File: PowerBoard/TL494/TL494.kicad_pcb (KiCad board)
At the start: 2 copper layers, 50 x 75 mm, 41 parts, among them J1 AuxConn, J2 POWER_SW, Q1 STD11N65M2, U2 LT8316EFE#PBF

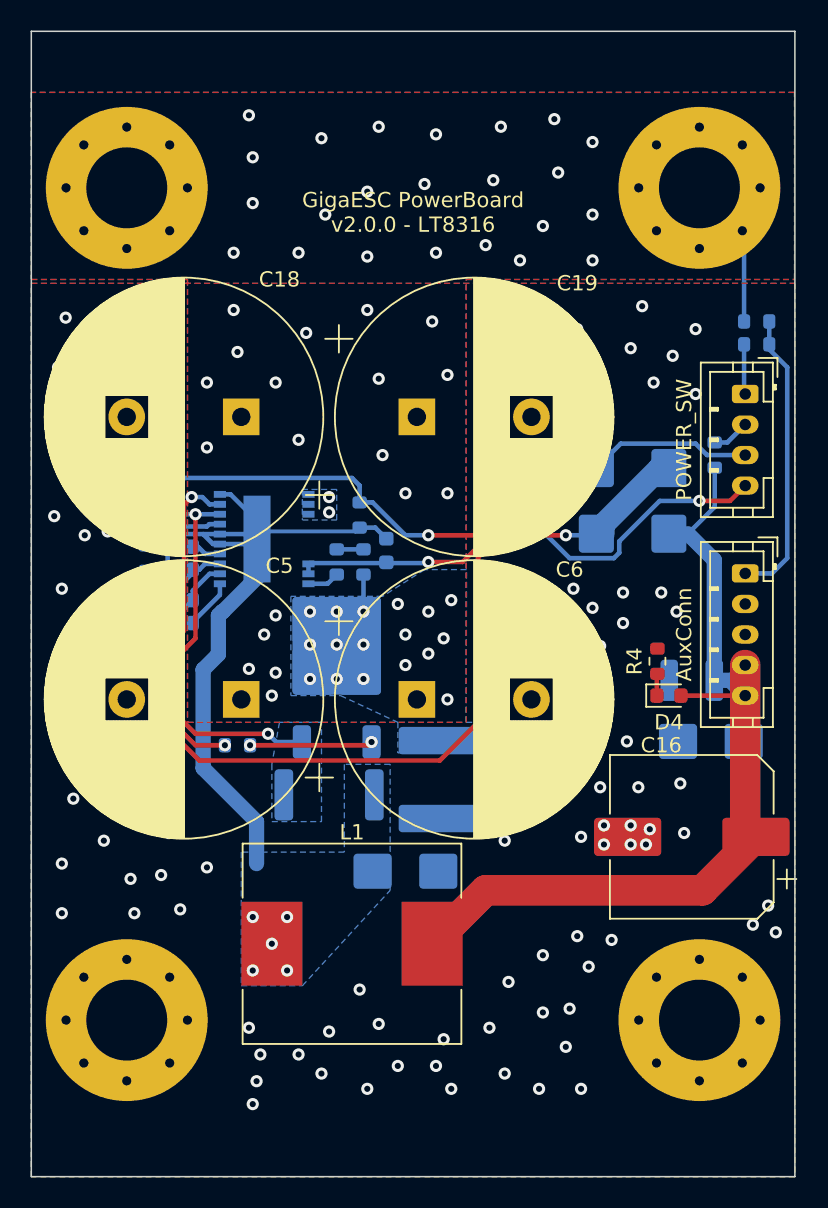
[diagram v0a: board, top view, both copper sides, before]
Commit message: v3.0.1 - GaN redesign
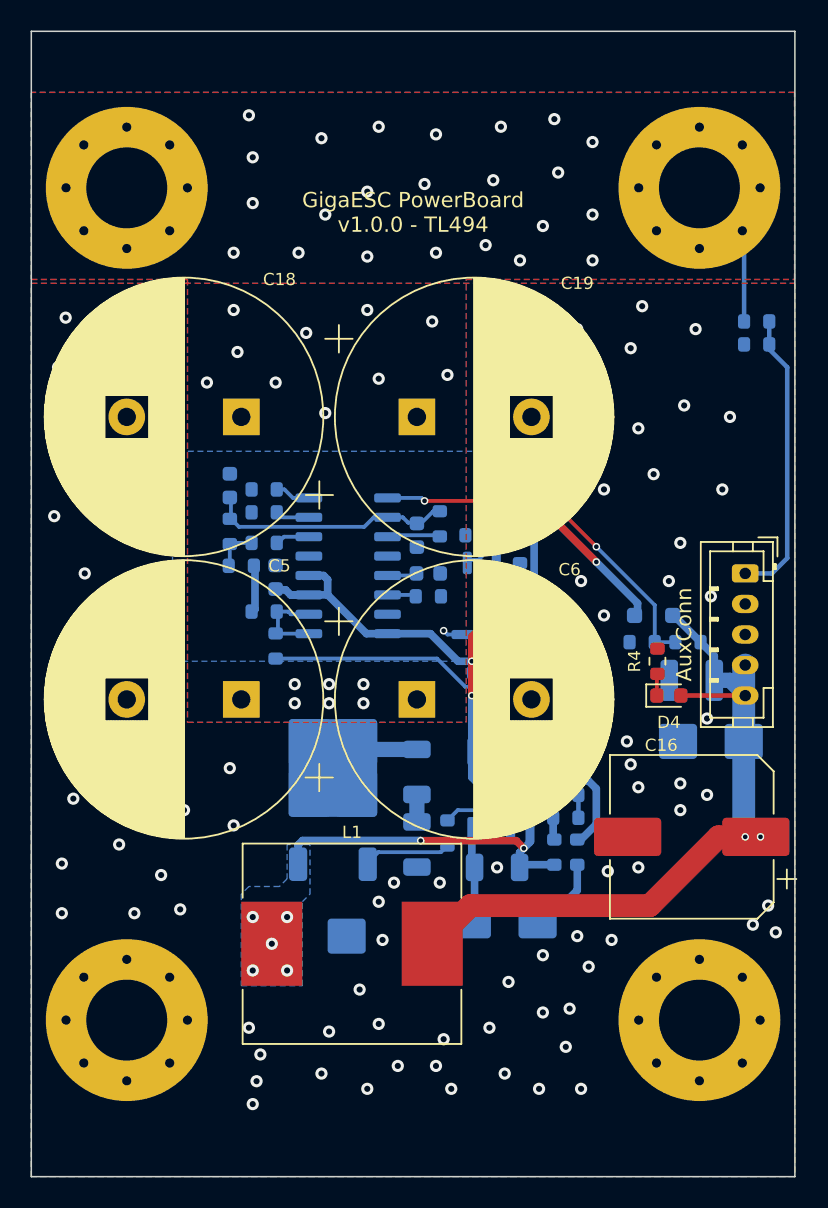
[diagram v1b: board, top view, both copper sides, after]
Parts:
- removed C10: 47p, GigaVescLibs:C_0603_1608Metric_L
- removed C13: 1n, Capacitor_SMD:C_0603_1608Metric
- removed J2: POWER_SW, Connector_JST:JST_PH_B4B-PH-K_1x04_P2.00mm_Vertical
- removed Q1: STD11N65M2, Package_TO_SOT_SMD:TO-252-2
- removed U2: LT8316EFE#PBF, GigaVescLibs:IC_LT8316EFE#PBF
- added C11: 1u, Capacitor_SMD:C_0603_1608Metric, B.Cu at (79.8, 117.0)
- added C3: 1n, Capacitor_SMD:C_0603_1608Metric, B.Cu at (76.0, 110.5)
- added C4: 100n, Capacitor_SMD:C_0603_1608Metric, B.Cu at (66.0, 110.8)
- added D3: BZT52C5V1S, Diode_SMD:D_SOD-323_HandSoldering, B.Cu at (82.5, 112.5)
- added Q2: BSS126, Package_TO_SOT_SMD:SOT-23, B.Cu at (79.2, 114.5)
- added Q5: IRFR13N20DTRPBF, Package_TO_SOT_SMD:TO-252-2, B.Cu at (69.8, 124.5)
- added R16: 10k, Resistor_SMD:R_0603_1608Metric, B.Cu at (82.0, 109.0)
- added R17: 100, Resistor_SMD:R_0603_1608Metric, B.Cu at (82.8, 115.5)
- added R18: 10k, Resistor_SMD:R_0603_1608Metric, B.Cu at (79.2, 108.0)
- added R19: 30k, Resistor_SMD:R_0603_1608Metric, B.Cu at (80.8, 105.0)
- added R20: 10k, Resistor_SMD:R_0603_1608Metric, B.Cu at (93.0, 115.0)
- added R21: 2.7k, Resistor_SMD:R_0603_1608Metric, B.Cu at (90.0, 115.0)
- added R22: 10k, Resistor_SMD:R_0603_1608Metric, B.Cu at (85.0, 126.5)
- added R23: 10k, Resistor_SMD:R_0603_1608Metric, B.Cu at (85.0, 125.0)
- added R7: 22, Resistor_SMD:R_0603_1608Metric, B.Cu at (85.8, 128.8)
- added R8: 1k, Resistor_SMD:R_0603_1608Metric, B.Cu at (84.2, 128.8)
- added TP1: TestPoint, TestPoint:TestPoint_Pad_1.0x1.0mm, B.Cu at (84.5, 123.0)
- added U1: TL494, Package_SO:SO-16_3.9x9.9mm_P1.27mm, B.Cu at (70.8, 110.0)
- added U3: IRS21271, Package_SO:SO-8_3.9x4.9mm_P1.27mm, B.Cu at (80.8, 124.8)
- added U4: TL431, Package_TO_SOT_SMD:SOT-23, B.Cu at (79.5, 110.8)
- C1: footprint GigaVescLibs:C_0603_1608Metric_L -> Capacitor_SMD:C_0603_1608Metric
- C12: value 47p -> 220n; footprint GigaVescLibs:C_0603_1608Metric_L -> Capacitor_SMD:C_1206_3216Metric
- C2: value 10u -> 10n
- C7: value 1u 200V -> 2.2u 100V; footprint Capacitor_SMD:C_2220_5650Metric -> Capacitor_SMD:C_1206_3216Metric
- C8: value 100n 200V -> 1n; footprint Capacitor_SMD:C_1206_3216Metric -> Capacitor_SMD:C_0603_1608Metric
- C9: value 100n -> 2.2u 100V; footprint GigaVescLibs:C_0603_1608Metric_L -> Capacitor_SMD:C_1206_3216Metric
- D6: value SS520BF -> 1N5819WS; footprint Diode_SMD:D_SMB -> Diode_SMD:D_SOD-323_HandSoldering
- L1: value 47uH -> 68uH
- R10: value 120k -> 5.1k
- R11: value 6.2k -> 5.1k
- R12: value 56k -> 20k
- R13: value 20 -> 22
- R14: value 100 -> 470
- R15: value 0.05 -> 100; footprint Resistor_SMD:R_2512_6332Metric -> Resistor_SMD:R_0603_1608Metric
- R5, R9: value 10k -> 100
- R6: value 10k -> 51k
- moved R5 31.3 mm to (66.0, 115.2), turned to 90 degrees
- moved D1 29.5 mm to (81.0, 133.2), turned to 0 degrees
- moved C9 25.8 mm to (75.2, 128.2), turned to -90 degrees
- moved C12 21.8 mm to (80.5, 129.8), turned to 0 degrees
- moved R6 20.6 mm to (76.8, 107.2), turned to -90 degrees
- moved R15 19.0 mm to (65.2, 106.5), turned to 0 degrees
- moved R12 16.3 mm to (76.0, 112.0)
- moved C8 16.3 mm to (80.8, 106.5), turned to 180 degrees
- moved C1 15.5 mm to (75.2, 108.0), turned to -90 degrees
- moved R13 14.9 mm to (77.2, 127.5), turned to -90 degrees
- moved C2 11.1 mm to (63.0, 104.8)
- moved R14 10.6 mm to (63.0, 107.8)
- moved R11 9.99 mm to (65.2, 108.5)
- moved R3 8.89 mm to (65.2, 113.0), turned to 180 degrees
- moved D6 8.39 mm to (90.8, 113.2), turned to 0 degrees
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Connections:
- C1 pad 1: Net-(U2-IREG/SS) -> Net-(U1-1IN-)
- C1 pad 2: GNDD -> -BATT
- C12 pad 1: +BATT -> Net-(D1-K)
- C12 pad 2: Net-(C12-Pad2) -> Net-(D2-K)
- C2 pad 1: Net-(D6-K) -> Net-(U1-1IN-)
- C2 pad 2: GNDD -> -BATT
- C7 pad 2: -BATT -> Net-(C7-Pad2)
- C8 pad 1: +BATT -> Net-(Q2-G)
- C8 pad 2: -BATT -> Net-(U4-R)
- C9 pad 1: Net-(C9-Pad1) -> Net-(C7-Pad2)
- C9 pad 2: GNDD -> -BATT
- D1 pad 2: +12V -> Net-(D1-A)
- D2 pad 1: GNDD -> Net-(D2-K)
- D6 pad 1: Net-(D6-K) -> BOOTSTRAP
- D6 pad 2: Net-(D1-K) -> +12V
- L1 pad 1: GNDD -> Net-(D2-K)
- R10 pad 1: Net-(U2-FB) -> Net-(R10-Pad1)
- R10 pad 2: Net-(U2-TC) -> -BATT
- R11 pad 1: Net-(U2-FB) -> Net-(U1-REF)
- R11 pad 2: GNDD -> Net-(R10-Pad1)
- R12 pad 1: Net-(D1-K) -> Net-(U1-RT)
- R12 pad 2: Net-(U2-FB) -> -BATT
- R14 pad 1: Net-(U2-SENSE) -> Net-(U1-1IN-)
- R14 pad 2: Net-(Q1-S) -> Net-(R10-Pad1)
- R15 pad 1: GNDD -> -BATT
- R15 pad 2: Net-(Q1-S) -> Net-(U1-2IN-)
- R3 pad 1: Net-(J2-Pin_4) -> Net-(U1-E1)
- R3 pad 2: GNDD -> -BATT
- R5 pad 2: +12V -> Net-(U1-E1)
- R6 pad 1: Net-(U2-VC) -> Net-(U1-1IN-)
- R6 pad 2: Net-(C9-Pad1) -> Net-(U1-FB)
- R9 pad 1: Net-(C12-Pad2) -> -BATT
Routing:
- net BOOTSTRAP: track 0.00 -> 63.5 mm, vias 0 -> 5
- net GNDD: track 58.1 -> 0.00 mm, vias 5 -> 0
- net Net-(J2-Pin_4): track 53.5 -> 0.00 mm, vias 5 -> 0
- net Net-(D1-K): track 56.8 -> 6.07 mm, vias 2 -> 0
- net Net-(D6-K): track 33.2 -> 0.00 mm, vias 2 -> 0
- net VFB: track 0.00 -> 24.3 mm, vias 0 -> 2
- net Net-(D2-K): track 0.00 -> 21.4 mm, vias 0 -> 7
- net Net-(U3-IN): track 2.49 -> 18.7 mm
- net Net-(U1-1IN-): track 0.00 -> 16.0 mm
- net +12V: track 62.7 -> 47.6 mm, vias 0 -> 2
- net Net-(U2-SENSE): track 14.2 -> 0.00 mm, vias 2 -> 0
- net Net-(U3-HO): track 21.8 -> 9.98 mm, vias 2 -> 0
- net Net-(Q1-S): track 10.1 -> 0.00 mm, vias 2 -> 0
- net Net-(Q2-G): track 0.00 -> 8.36 mm
- net Net-(D3-K): track 0.00 -> 7.42 mm
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- added copper zone on B.Cu, net Net-(D2-K)
- removed copper zone on B.Cu, net GNDD
- removed copper zone on B.Cu, net Net-(Q1-S)
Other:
- board text added: "GigaESC PowerBoard v1.0.0 - TL494"
- board text removed: "GigaESC PowerBoard v2.0.0 - LT8316"

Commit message: v3.0.2 - Prerelease
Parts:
- added C10: 22u, Capacitor_SMD:C_1206_3216Metric, F.Cu at (89.8, 130.5)
- added C13: 22u, Capacitor_SMD:C_1206_3216Metric, F.Cu at (87.2, 130.5)
- added C14: 22u, Capacitor_SMD:C_1206_3216Metric, F.Cu at (84.8, 133.5)
- added C17: 22u, Capacitor_SMD:C_1206_3216Metric, F.Cu at (82.2, 133.5)
- C16: value 470u 25V -> 22u; footprint Capacitor_SMD:CP_Elec_10x10.5 -> Capacitor_SMD:C_1206_3216Metric
- C2: value 10n -> 22u; footprint Capacitor_SMD:C_0603_1608Metric -> Capacitor_SMD:C_1206_3216Metric; moved to F.Cu
- L1: value 68uH -> 100uH
- R12: value 20k -> 5.1k
- R14: value 470 -> 200k
- R15: value 100 -> 10k
- R6: value 51k -> 2k
- moved C2 39.0 mm to (92.2, 130.5)
- moved C16 14.7 mm to (79.8, 133.5), turned to -90 degrees
- moved R15 10.8 mm to (76.0, 106.0), turned to 180 degrees
- moved R14 2.37 mm to (65.2, 107.0), turned to 180 degrees
- moved C1 1.25 mm to (76.0, 109.0), turned to 180 degrees
- moved R6 0.79 mm to (76.0, 107.5), turned to 0 degrees
- moved R9 0.50 mm to (65.2, 105.5)
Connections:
- C1 pad 1: Net-(U1-1IN-) -> Net-(C1-Pad1)
- C1 pad 2: -BATT -> Net-(U1-FB)
- C2 pad 1: Net-(U1-1IN-) -> +12V
- R15 pad 1: -BATT -> Net-(U1-FB)
- R6 pad 2: Net-(U1-FB) -> Net-(C1-Pad1)
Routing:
- net Net-(U1-1IN-): track 16.0 -> 9.82 mm
- net Net-(U1-2IN-): track 2.10 -> 7.34 mm
- net Net-(U1-FB): track 3.47 -> 5.94 mm
- net Net-(C1-Pad1): track 0.00 -> 1.52 mm
- net Net-(R10-Pad1): track 2.91 -> 4.41 mm

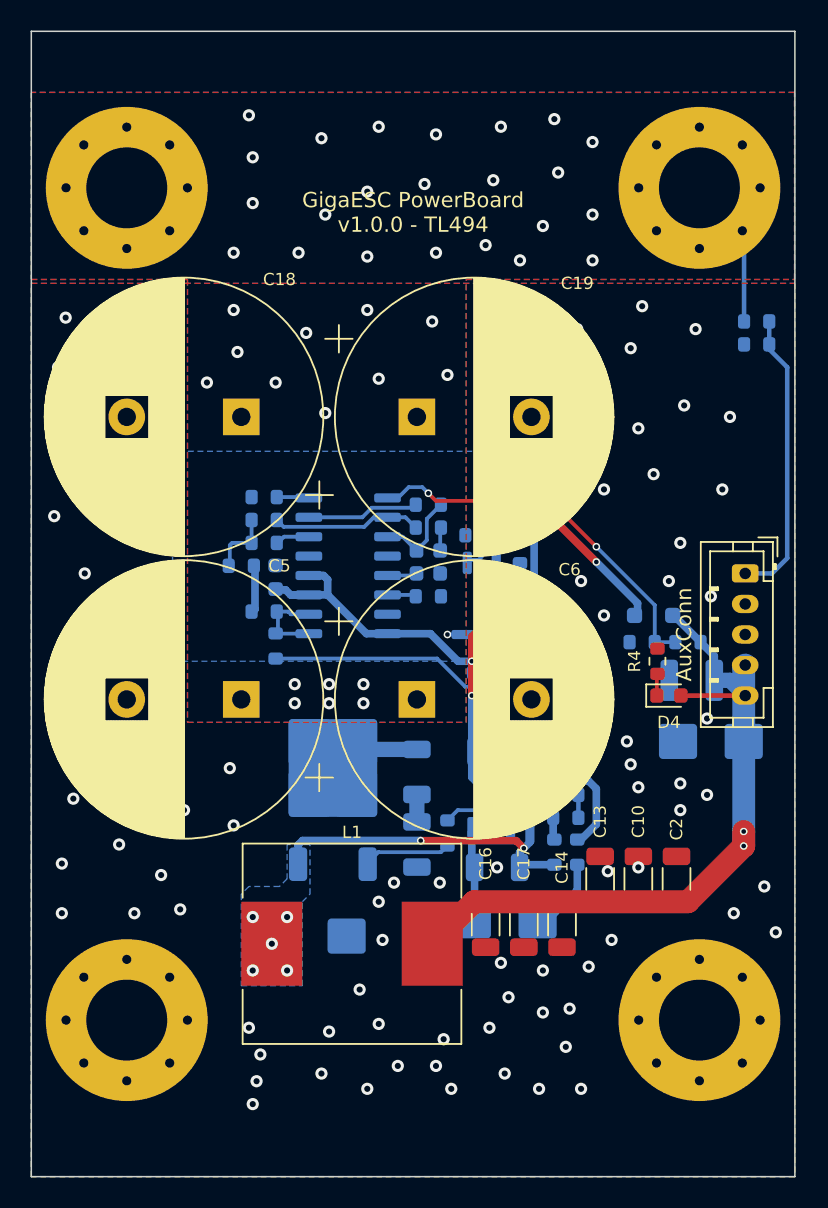
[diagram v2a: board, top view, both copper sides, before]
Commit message: v3.1.0 - Power supply fixes
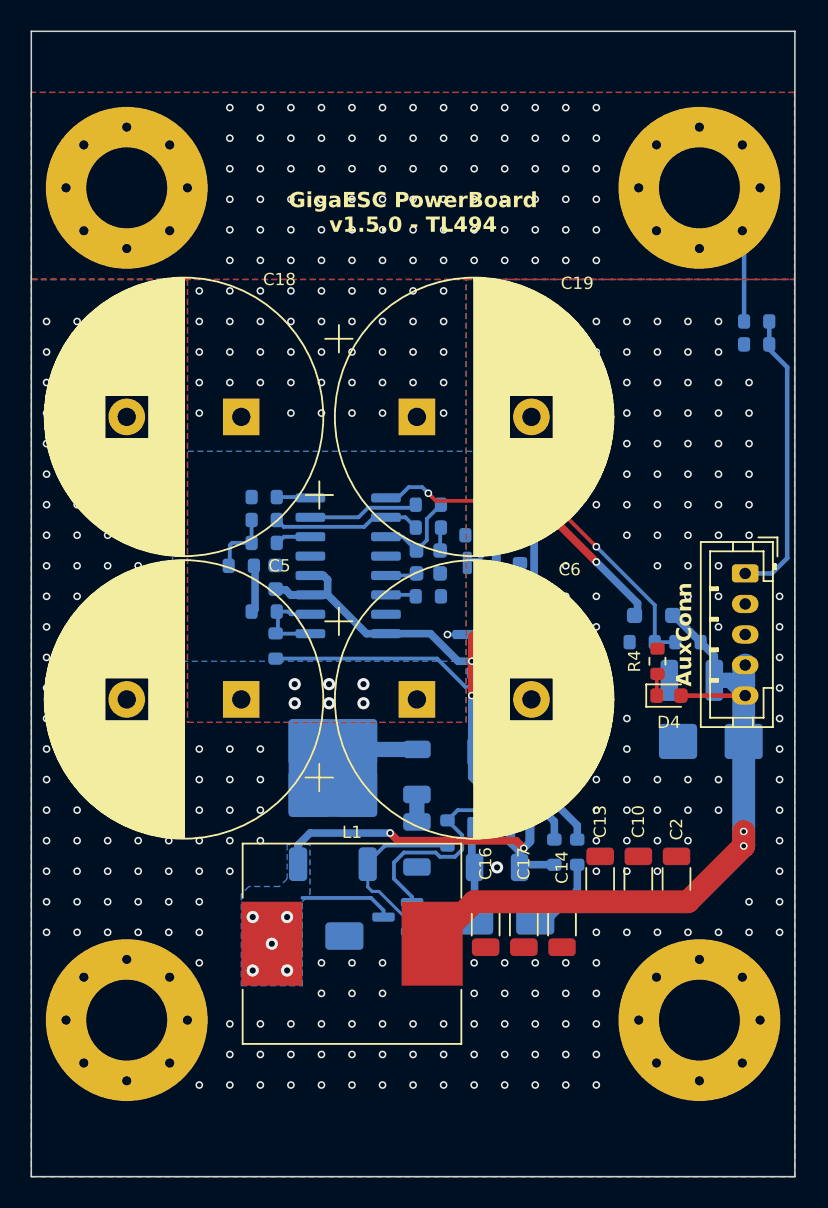
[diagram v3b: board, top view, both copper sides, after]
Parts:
- removed R22, R23: 10k, Resistor_SMD:R_0603_1608Metric
- added Q1: S9012 2T1, Package_TO_SOT_SMD:SOT-23, B.Cu at (74.0, 133.0)
- D1, D2: value SS520BF -> SS520F; footprint Diode_SMD:D_SMB -> Diode_SMD:D_SMA
- U1: footprint Package_SO:SO-16_3.9x9.9mm_P1.27mm -> Package_SO:SOIC-16_3.9x9.9mm_P1.27mm
- moved Q2 0.06 mm to (79.2, 114.5)
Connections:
- R13 pad 1: Net-(U3-HO) -> Net-(Q1-B)
- R8 pad 2: Net-(U3-CS) -> Net-(Q1-B)
- U3 pad 6: Net-(U3-CS) -> Net-(D2-K)
- U3 pad 7: Net-(U3-HO) -> Net-(Q1-B)
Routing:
- net Net-(Q1-B): track 0.00 -> 21.5 mm
- net Net-(U3-HO): track 9.98 -> 0.00 mm
- net Net-(D2-K): track 21.4 -> 30.6 mm
- net Net-(Q1-E): track 5.69 -> 11.6 mm
- net Net-(U3-CS): track 5.56 -> 0.00 mm
- net BOOTSTRAP: track 63.8 -> 60.5 mm
- net Net-(R22-Pad2): track 1.50 -> 0.00 mm
- net -BATT: vias 93 -> 276
- net +BATT: vias 40 -> 127
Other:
- board text added: "GigaESC PowerBoard v1.5.0 - TL494"
- board text removed: "GigaESC PowerBoard v1.0.0 - TL494"
